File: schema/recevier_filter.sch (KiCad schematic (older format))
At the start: 16 parts, among them U7 LMC6482, U8 LM393

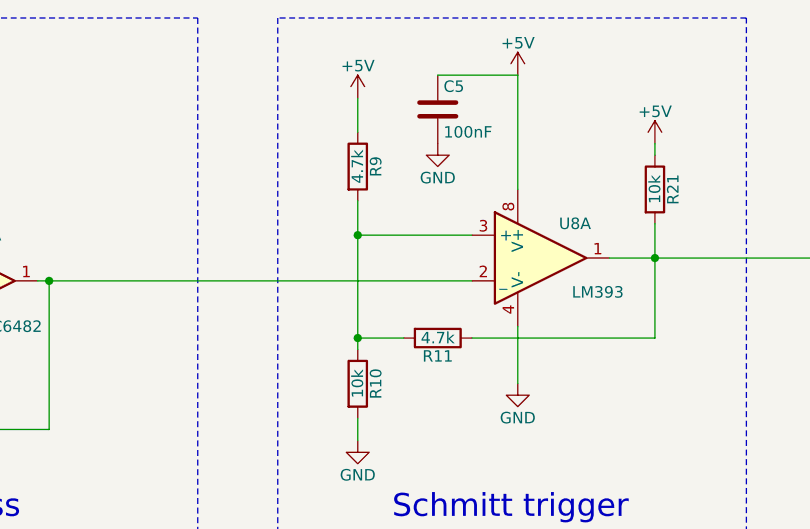
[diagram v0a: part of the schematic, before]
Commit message: fix schmitt trigger
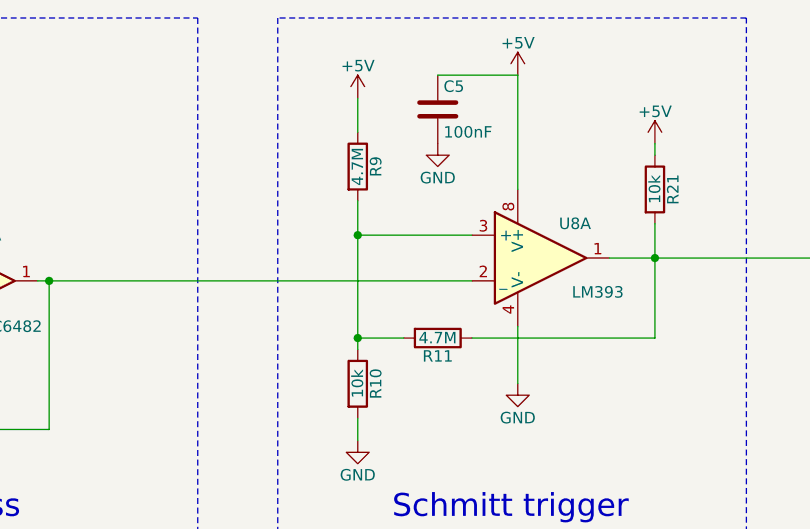
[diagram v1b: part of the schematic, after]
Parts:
- R11, R9: value 4.7k -> 4.7M
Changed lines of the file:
@@
 $Descr A4 11693 8268
 encoding utf-8
-Sheet 3 6
+Sheet 4 6
 Title "Recevier / Filter"
 Date ""
@@
 P 7600 3050
 F 0 "R9" V 7680 3050 50  0000 C CNN
-F 1 "4.7k" V 7600 3050 50  0000 C CNN
+F 1 "4.7M" V 7600 3050 50  0000 C CNN
 F 2 "" V 7530 3050 50  0000 C CNN
 F 3 "" H 7600 3050 50  0000 C CNN
@@
 P 7950 3800
 F 0 "R11" V 8030 3800 50  0000 C CNN
-F 1 "4.7k" V 7950 3800 50  0000 C CNN
+F 1 "4.7M" V 7950 3800 50  0000 C CNN
 F 2 "" V 7880 3800 50  0000 C CNN
 F 3 "" H 7950 3800 50  0000 C CNN
